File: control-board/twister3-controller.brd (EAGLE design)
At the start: 191 x 90.5 mm, 54 parts, among them J2 OSTVN04A150, J7 BARREL-JACK_PJ-063BH, U1 MAX6816, U10 Teensy 3.2, U11 TMC2130-LA, U2 GDM1602K, U3 IS31FL3193, U4 MIC4680-5.0YM-TR

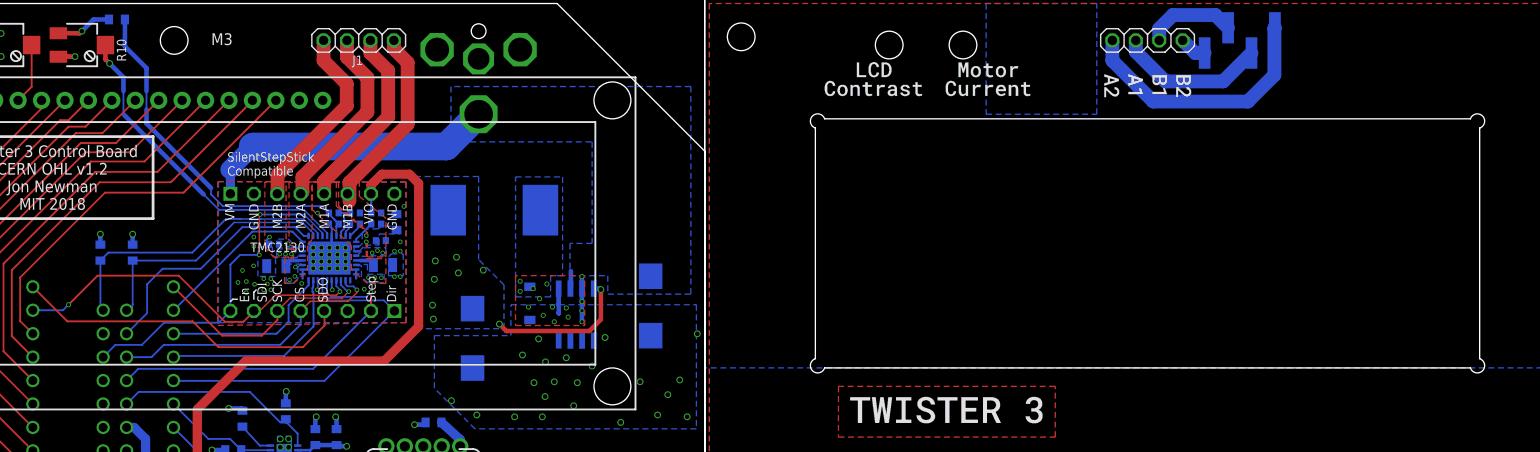
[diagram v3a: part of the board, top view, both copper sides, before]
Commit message: Small updates to control board
- Tighter tolerance on LCD cutout
- Added test points
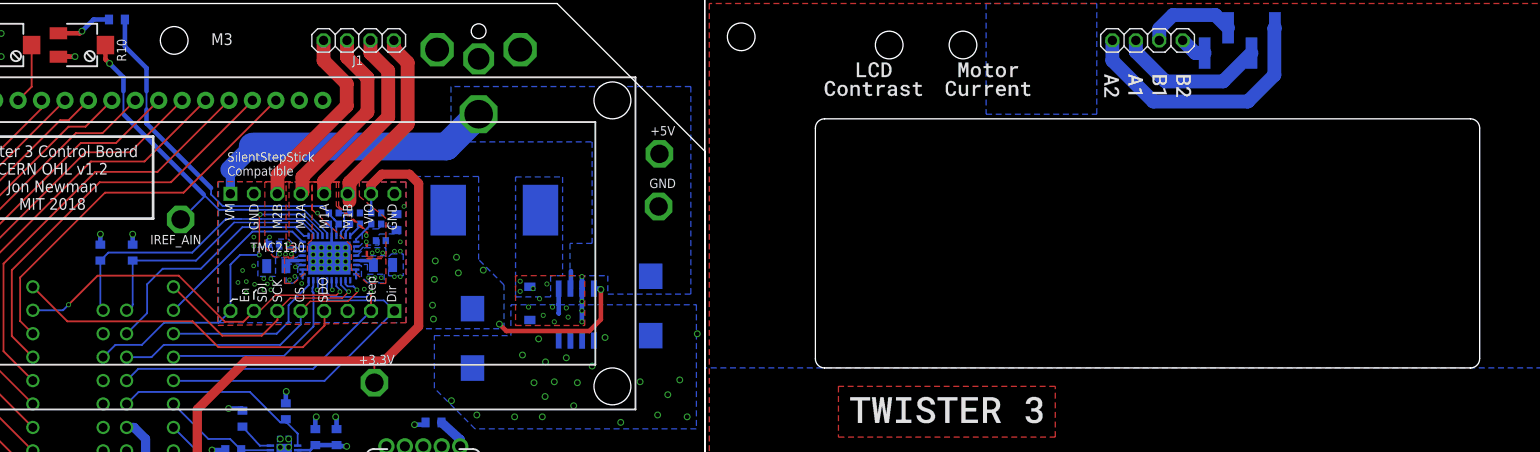
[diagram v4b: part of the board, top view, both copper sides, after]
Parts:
- added +3.3V, +5V, GND, IREF_AIN: (no value), jonnew:TESTPOINT_2MM
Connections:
- net +3V3: now also +3.3V.1
- net +5V0: now also +5V.1
- net GND: now also GND.1
- net IREF: now also IREF_AIN.1
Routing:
- net IREF: track 36.4 -> 40.1 mm
- net +3V3: track 86.4 -> 88.8 mm
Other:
- board text added: "+3.3V"
- board text added: "+5V"
- board text added: "IREF_AIN"
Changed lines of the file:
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@@
 <setting verticaltext="up"/>
 </settings>
-<grid distance="0.5" unitdist="mm" unit="mm" style="lines" multiple="1" display="yes" altdistance="5" altunitdist="mil" altunit="mil"/>
+<grid distance="0.1" unitdist="mm" unit="mm" style="lines" multiple="1" display="yes" altdistance="5" altunitdist="mil" altunit="mil"/>
 <layers>
 <layer number="1" name="Top" color="4" fill="1" visible="yes" active="yes"/>
@@
 <layer number="27" name="tValues" color="7" fill="1" visible="yes" active="yes"/>
 <layer number="28" name="bValues" color="7" fill="1" visible="yes" active="yes"/>
-<layer number="29" name="tStop" color="7" fill="3" visible="no" active="yes"/>
-<layer number="30" name="bStop" color="7" fill="6" visible="no" active="yes"/>
-<layer number="31" name="tCream" color="7" fill="4" visible="no" active="yes"/>
-<layer number="32" name="bCream" color="7" fill="5" visible="no" active="yes"/>
+<layer number="29" name="tStop" color="7" fill="3" visible="yes" active="yes"/>
+<layer number="30" name="bStop" color="7" fill="6" visible="yes" active="yes"/>
+<layer number="31" name="tCream" color="7" fill="4" visible="yes" active="yes"/>
+<layer number="32" name="bCream" color="7" fill="5" visible="yes" active="yes"/>
 <layer number="33" name="tFinish" color="6" fill="3" visible="no" active="yes"/>
 <layer number="34" name="bFinish" color="6" fill="6" visible="no" active="yes"/>
@@
 <wire x1="-1" y1="0" x2="1" y2="0" width="0.127" layer="51"/>
 <wire x1="107.5" y1="53.5" x2="107.5" y2="28.5" width="0" layer="20"/>
+<wire x1="107.5" y1="28.5" x2="108.5" y2="27.5" width="0" layer="20" curve="90"/>
 <wire x1="108.5" y1="27.5" x2="178.5" y2="27.5" width="0" layer="20"/>
+<wire x1="178.5" y1="27.5" x2="179.5" y2="28.5" width="0" layer="20" curve="90"/>
 <wire x1="179.5" y1="28.5" x2="179.5" y2="53.5" width="0" layer="20"/>
 <circle x="160.5" y="12" radius="3.3" width="0.05" layer="20"/>
 <wire x1="178.5" y1="54.5" x2="108.5" y2="54.5" width="0" layer="20"/>
-<wire x1="107.5" y1="53.5" x2="108.5" y2="54.5" width="0" layer="20" curve="-233.130102"/>
-<wire x1="108.5" y1="27.5" x2="107.5" y2="28.5" width="0" layer="20" curve="-233.130102"/>
-<wire x1="179.5" y1="28.5" x2="178.5" y2="27.5" width="0" layer="20" curve="-233.130102"/>
-<wire x1="178.5" y1="54.5" x2="179.5" y2="53.5" width="0" layer="20" curve="-233.130102"/>
 <wire x1="95.5" y1="81" x2="95.5" y2="-9.5" width="0" layer="20"/>
 <text x="92.5" y="82" size="1.778" layer="20">V-CUT</text>
@@
 <circle x="133.5" y="63" radius="3.5" width="0" layer="32"/>
 <text x="135.5" y="58" size="1.27" layer="22" font="vector" ratio="18" rot="MR0">M5</text>
+<wire x1="107.5" y1="53.5" x2="108.5" y2="54.5" width="0" layer="20" curve="-90"/>
+<wire x1="178.5" y1="54.5" x2="179.5" y2="53.5" width="0" layer="20" curve="-90"/>
+<text x="41.4" y="40.9" size="1.016" layer="22" font="vector" ratio="18" rot="MR0">IREF_AIN</text>
+<text x="61.8" y="27.8" size="1.016" layer="22" font="vector" ratio="18" rot="MR0">+3.3V</text>
+<text x="92" y="52.7" size="1.016" layer="22" font="vector" ratio="18" rot="MR0">+5V</text>
+<text x="92.4" y="46.9" size="1.016" layer="22" font="vector" ratio="18" rot="MR0">GND</text>
 </plain>
 <attributes>
@@
 <attribute name="VALUE" x="83.601971875" y="3.71381875" size="1.27" layer="27" font="vector" ratio="18" rot="R45"/>
 </element>
+<element name="GND" library="jonnew" package="TESTPOINT_2MM" value="" x="90.5" y="45" smashed="yes">
+<attribute name="NAME" x="89.5" y="47" size="1.016" layer="25" font="vector" ratio="18"/>
+<attribute name="VALUE" x="89.5" y="42" size="0.8128" layer="27" font="vector" ratio="18"/>
+</element>
+<element name="+5V" library="jonnew" package="TESTPOINT_2MM" value="" x="90.6" y="50.7" smashed="yes">
+<attribute name="NAME" x="89.6" y="52.7" size="1.016" layer="25" font="vector" ratio="18"/>
+<attribute name="VALUE" x="89.6" y="47.7" size="0.8128" layer="27" font="vector" ratio="18"/>
+</element>
+<element name="+3.3V" library="jonnew" package="TESTPOINT_2MM" value="" x="59.7" y="25.9" smashed="yes">
+<attribute name="NAME" x="58" y="27.9" size="1.016" layer="25" font="vector" ratio="18"/>
+<attribute name="VALUE" x="58.7" y="22.9" size="0.8128" layer="27" font="vector" ratio="18"/>
+</element>
+<element name="IREF_AIN" library="jonnew" package="TESTPOINT_2MM" value="" x="38.7" y="43.6" smashed="yes">
+<attribute name="NAME" x="35.4" y="40.9" size="1.016" layer="25" font="vector" ratio="18"/>
+<attribute name="VALUE" x="37.7" y="40.6" size="0.8128" layer="27" font="vector" ratio="18"/>
+</element>
 </elements>
 <signals>
@@
 <wire x1="34.9" y1="19.8" x2="34.9" y2="17.95" width="1" layer="16"/>
 <wire x1="34.9" y1="17.95" x2="33.5" y2="16.55" width="1" layer="16"/>
-<wire x1="45.75" y1="28.25" x2="60.75" y2="28.25" width="1" layer="1"/>
+<wire x1="59.6" y1="28.25" x2="45.75" y2="28.25" width="1" layer="1"/>
+<wire x1="59.6" y1="28.25" x2="60.75" y2="28.25" width="1" layer="1"/>
 <wire x1="40.5" y1="23" x2="45.75" y2="28.25" width="1" layer="1"/>
+<contactref element="+3.3V" pad="1"/>
+<wire x1="59.7" y1="25.9" x2="59.7" y2="28.008578125" width="0.2" layer="1"/>
+<wire x1="59.7" y1="28.008578125" x2="59.6" y2="28.25" width="0.2" layer="1" curve="45"/>
 </signal>
 <signal name="N$4">
@@
 <wire x1="19.25" y1="61.25" x2="17.45" y2="61.25" width="0.5" layer="1"/>
 <wire x1="17.45" y1="61.25" x2="17.45" y2="61.23" width="0.5" layer="1"/>
-<wire x1="25.27" y1="61.23" x2="25.5" y2="61.23" width="0.3" layer="1"/>
+<wire x1="25.45" y1="61.23" x2="25.5" y2="61.23" width="0.3" layer="1"/>
 <wire x1="25.45" y1="61.23" x2="25.27" y2="61.23" width="0.3" layer="1"/>
+<contactref element="GND" pad="1"/>
 </signal>
 <signal name="ENC_A">
@@
 <wire x1="46.7" y1="44.6341" x2="46.7" y2="44.6" width="0.2" layer="16"/>
 <wire x1="46.7" y1="44.6341" x2="42.8659" y2="44.6341" width="0.2" layer="16"/>
-<wire x1="42.8659" y1="44.6341" x2="41.2" y2="46.3" width="0.2" layer="16"/>
+<wire x1="41.35" y1="46.15" x2="42.8659" y2="44.6341" width="0.2" layer="16"/>
+<wire x1="41.35" y1="46.15" x2="41.2" y2="46.3" width="0.2" layer="16"/>
 <wire x1="52.07161875" y1="44.6341" x2="46.7" y2="44.6341" width="0.2" layer="16"/>
 <wire x1="54.574" y1="41.81" x2="54.574" y2="42.13171875" width="0.16" layer="16"/>
@@
 <wire x1="31" y1="60.5" x2="30.55" y2="60.95" width="0.5" layer="1"/>
 <wire x1="30.55" y1="60.95" x2="30.55" y2="62.5" width="0.5" layer="1"/>
+<contactref element="IREF_AIN" pad="1"/>
+<wire x1="38.7" y1="43.6" x2="38.870709375" y2="43.670709375" width="0.2" layer="16" curve="44.999476"/>
+<wire x1="38.870709375" y1="43.670709375" x2="41.35" y2="46.15" width="0.2" layer="16"/>
 </signal>
 <signal name="CFG-6">
@@
 <wire x1="54.1" y1="15.0636" x2="52.2236" y2="15.0636" width="0.3" layer="16"/>
 <wire x1="52.2236" y1="15.0636" x2="52.16" y2="15" width="0.3" layer="16"/>
+<contactref element="+5V" pad="1"/>
 </signal>
 <signal name="V_BM">

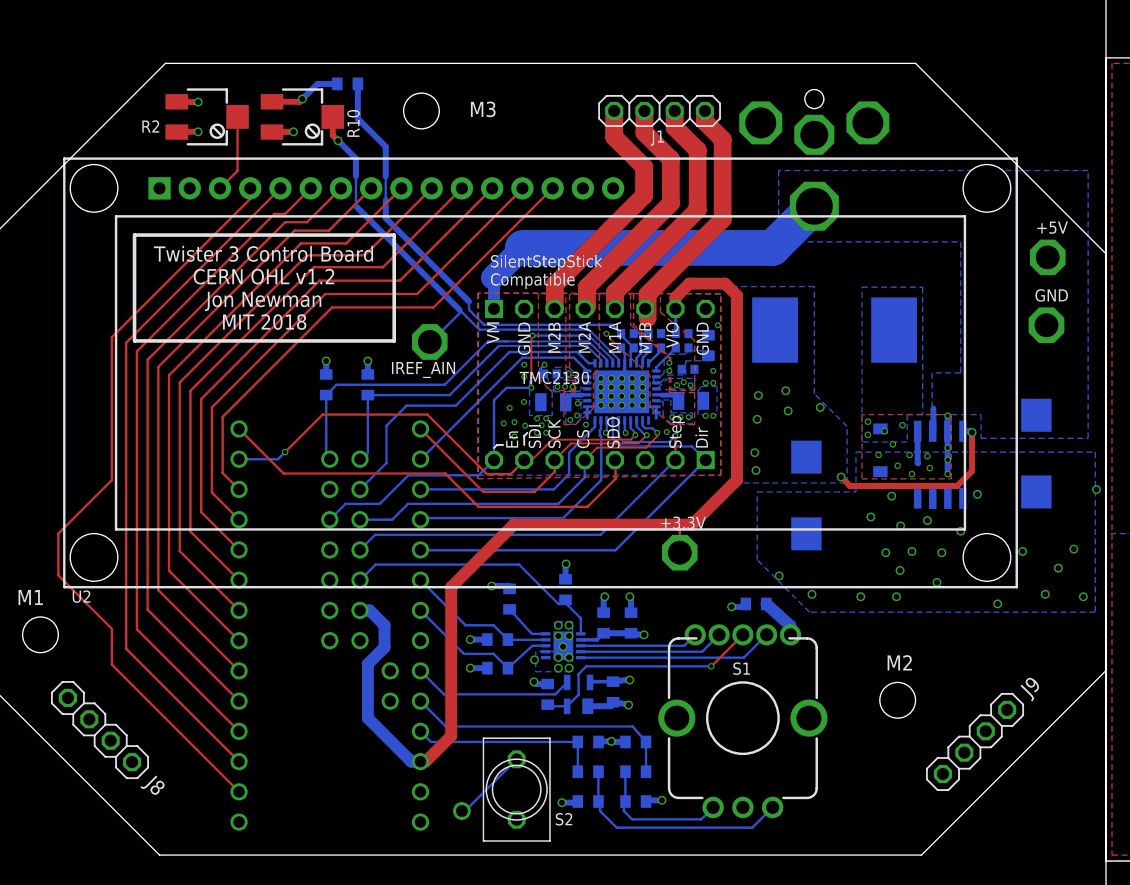
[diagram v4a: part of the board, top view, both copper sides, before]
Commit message: Updates to control board after assembly of rev 1.1
- Better retaining mechanism for top panel
- Simplified and updated BOM on the google doc to match this version
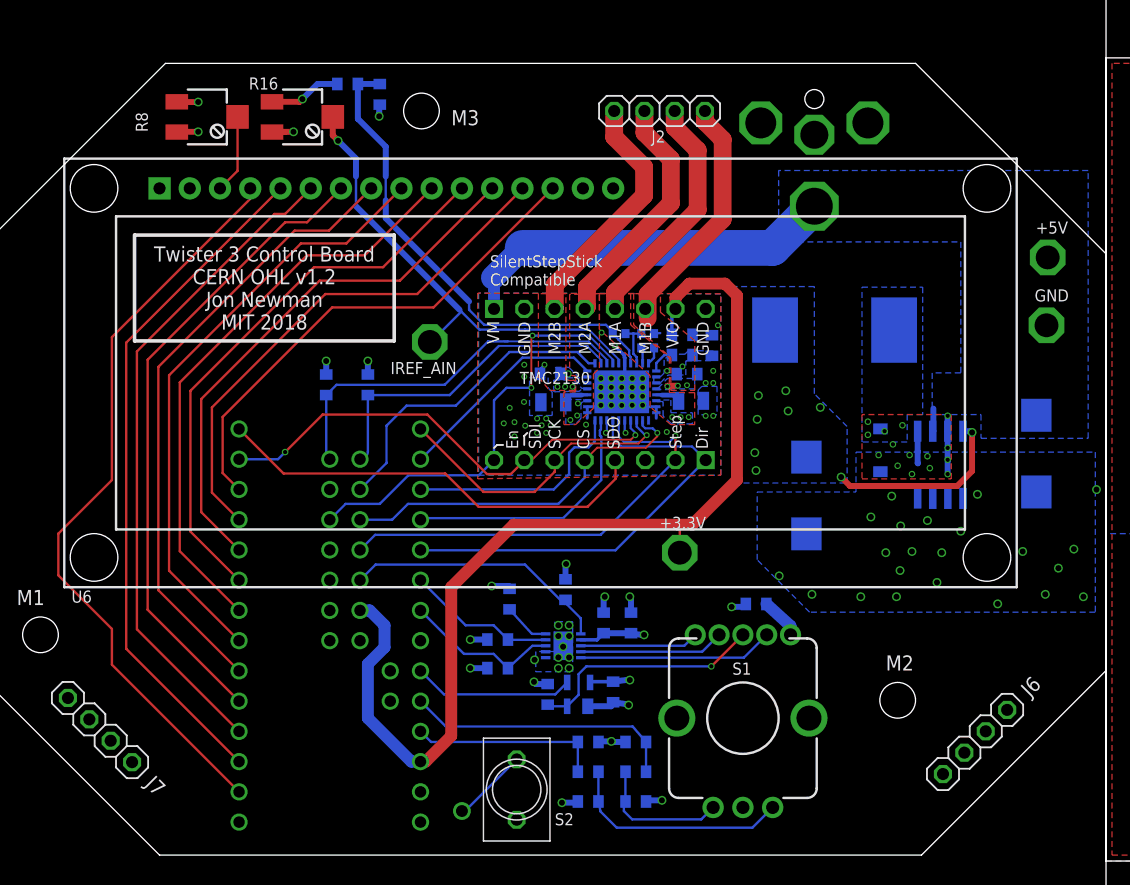
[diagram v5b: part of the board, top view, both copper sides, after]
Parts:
- removed C17: 100n/50V, jonnew:0402
- removed C18: 100nF/50V, jonnew:0402
- removed C19: 22nF/50V, jonnew:0402
- removed R18, R19: 0.11, jonnew:0805
- removed R22: 20k, jonnew:0603
- removed R23: 2.2, jonnew:0402
- removed U11: TMC2130-LA, we-chip:QFN36-PAD
- added C10, C9: 100nF/50V, jonnew:0603
- added C11: 1uF/50V, jonnew:0603
- added R11: 4.7k, cyclops:0603
- added R17: 10k, jonnew:0603
- added R8: 20k, jonnew:SM-42/43X
- added R9: 4.7k, jonnew:0603
- added U6: GDM1602K, jonnew:LCD-16X2
- C12: value 1u/50V -> 100nF/50V
- C13: value 100n/50V -> 22nF/50V
- C14: value 470nF/10V -> 1uF/50V; device jonnew:0402 -> jonnew:0603
- C15: value 47uF/10V -> 100nF/50V; device jonnew:0402 -> jonnew:0603
- C16: value 100n/50V -> 470nF/10V
- C3: value 10nF -> 1uF/50V
- C4: value 10nF -> T491D156K035AT; device jonnew:0603 -> jonnew:7343M
- C5: value 10nF -> T491D227M010AT; device jonnew:0603 -> jonnew:7343M
- C6: value 1uF -> 10nF
- C7: value T491D227M010AT -> 10nF; device jonnew:7343M -> jonnew:0603
- C8: value T491D156K035AT -> 10nF; device jonnew:7343M -> jonnew:0603
- J1: value (none) -> BARREL-JACK_PJ-063BH; device jonnew:1X04 -> jonnew:PJ-063BH
- J2: value OSTVN04A150 -> (none)
- J5: value (none) -> OSTVN04A150; device jonnew:JP4_SMD -> jonnew:1X04
- J7: value BARREL-JACK_PJ-063BH -> (none); device jonnew:PJ-063BH -> jonnew:1X04
- J8: device jonnew:1X04 -> jonnew:JP4_SMD
- R1: value 10k -> 4.7k
- R10: value 20k -> 4.7k; device jonnew:SM-42/43X -> jonnew:0603
- R12: device jonnew:0603 -> cyclops:0603
- R13: value 470 -> 20k; device cyclops:0603 -> jonnew:0603
- R14, R15: value 4.7k -> 0.11; device cyclops:0603 -> jonnew:0805
- R16: value 100k -> 20k; device jonnew:0603 -> jonnew:SM-42/43X
- R2: value 20k -> 10k; device jonnew:SM-42/43X -> jonnew:0603
- R3: value 4.7k -> 10k
- R6: value 10k -> 470; device jonnew:0603 -> cyclops:0603
- R7: value 4.7k -> 2.2; device jonnew:0603 -> jonnew:0402
- U1: value MAX6816 -> IS31FL3193; device jonnew:SOT143-4 -> jonnew:PWSON-N10-3X3
- U2: value GDM1602K -> MIC4680-5.0YM-TR; device jonnew:LCD-16X2 -> jonnew:SOIC127P500X400-8N
- U3: value IS31FL3193 -> MAX6816; device jonnew:PWSON-N10-3X3 -> jonnew:SOT143-4
- U4: value MIC4680-5.0YM-TR -> TMC2130-LA; device jonnew:SOIC127P500X400-8N -> we-chip:QFN36-PAD
- moved J8 151.7 mm to (153.5, 63.0), flipped to the bottom, turned to 180 degrees
- moved J2 85.5 mm to (58.0, 63.0), turned to 180 degrees
- moved J7 82.1 mm to (11.0, 11.0), flipped to the top, turned to 135 degrees
- moved J4 73.5 mm to (180.0, 10.0), turned to 315 degrees
- moved J3 70.1 mm to (106.5, 11.0), turned to 225 degrees
- moved R2 67.8 mm to (56.0, 5.00), flipped to the bottom, turned to 180 degrees
- moved J5 64.4 mm to (143.5, 63.0), flipped to the top, turned to 0 degrees
- moved R13 54.0 mm to (31.8, 65.3), turned to 180 degrees
- moved R10 49.1 mm to (44.4, 16.2), flipped to the bottom, turned to 180 degrees
- moved R16 45.4 mm to (28.0, 62.5), flipped to the top, turned to 270 degrees
- moved C4 40.8 mm to (89.6, 34.2)
- moved C8 40.8 mm to (54.1, 14.2)
- moved U2 34.5 mm to (81.6, 33.3), flipped to the bottom, turned to 270 degrees
- moved C14 30.6 mm to (34.5, 64.4), turned to 90 degrees
- moved R7 29.9 mm to (54.6, 44.3), turned to 0 degrees
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- renumbered J9 to J6, JP6 to J10, JP7 to J11, U10 to U5
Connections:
- net !IS31_SHDN: now also R17.1, U1.1; no longer R16.1, U3.1
- net +24V0: now also C10.1, C11.1, C4.+, C9.1, J1.1, U2.2, U4.16, U4.30, U4.31; no longer C16.1, C17.1, C18.1, C8.+, J7.1, U11.16, U11.30, U11.31, U4.2
- net +3V3: now also C15.2, U4.8; no longer C13.2, U11.8
- net +5V0: now also C2.1, C3.1, C5.+, C8.1, R10.1, R11.2, R2.2, R3.2, R8.1, R9.1, U1.2, U2.4, U3.4, U6.15, U6.2; no longer C4.1, C5.1, C6.1, C7.+, R14.2, R15.2, R2.1, R3.1, R6.2, R7.1, U1.4, U2.15, U2.2, U3.2, U4.4
- net +5VOUT: now also C14.2, R13.2, R7.2, U4.25; no longer C15.2, R22.2, R23.2, U11.25
- net BRA1: now also R15.2, U4.33; no longer R19.2, U11.33
- net BRB1: now also R14.2, U4.14; no longer R18.2, U11.14
- net BUTT: now also U3.3; no longer U1.3
- net CFG-0/MISO: now also U4.5; no longer U11.5
- net CFG-1/MOSI: now also U4.4; no longer U11.4
- net CFG-2/SCLK: now also U4.3; no longer U11.3
- net CFG-3/!TMC_CS: now also U4.2; no longer U11.2
- net CFG-6: now also U4.22; no longer U11.22
- net CFG4: now also U4.18; no longer U11.18
- net CFG5: now also U4.19; no longer U11.19
- net CPI1: now also C13.2, U4.28; no longer C19.2, U11.28
- net CPO1: now also C13.1, U4.27; no longer C19.1, U11.27
- net DB0: now also U6.7; no longer U2.7
- net DB1: now also U6.8; no longer U2.8
- net DB2: now also U6.9; no longer U2.9
- net DB3: now also U6.10; no longer U2.10
- net DB4: now also U6.11; no longer U2.11
- net DB5: now also U6.12; no longer U2.12
- net DB6: now also U6.13; no longer U2.13
- net DB7: now also U6.14; no longer U2.14
- net DIAG0: now also R11.1, U4.20; no longer R15.1, U11.20
- net DIAG1: now also R12.1, U4.21; no longer R14.1, U11.21
- net DIR: now also U4.7; no longer U11.7
- net E: now also U6.6; no longer U2.6
- net ENC_A: now also C6.1, R4.2; no longer C3.1, R5.2
- net ENC_B: now also C7.1, R5.2; no longer C2.1, R4.2
- net GND: now also C10.2, C11.2, C16.1, C4.-, C5.-, C7.2, C8.2, C9.2, J1.2, R14.1, R15.1, R16.3, R17.2, R6.1, R8.3, U1.6, U1.7, U1.PAD, U2.5, U2.6, U2.7, U2.8, U3.1, U4.11, U4.12, U4.24, U4.35, U4.36, U4.TP, U6.1, U6.16; no longer C12.2, C13.1, C16.2, C17.2, C4.2, C5.2, C7.-, C8.-, J7.2, R10.3, R13.1, R16.2, R18.1, R19.1, R2.3, U1.1, U11.1, U11.11, U11.12, U11.24, U11.35, U11.36, U11.TP, U2.16, U3.6, U3.7, U3.PAD, U4.5, U4.6, U4.7, U4.8
- net IREF: now also R16.2, U4.23; no longer R10.2, U11.23
- net MECH: now also J3.1, J3.2, J3.3, J3.4; no longer J5.1, J5.2, J5.3, J5.4
- net N$1: now also R2.1, R4.1; no longer R1.1, R5.1
- net N$10: now also U1.4; no longer U3.4
- net N$11: now also R8.2, U6.3; no longer R2.2, U2.3
- net N$2: now also R6.2, U3.2; no longer R13.2, U1.2
- net N$3: now also U1.3; no longer U3.3
- net N$4: now also R3.1, R5.1; no longer R4.1, R6.1
- net N$6: now also J5.1, J8.4; no longer J2.1, J3.4
- net N$7: now also J5.2, J8.3; no longer J2.2, J3.3
- net N$8: now also J5.3, J8.2; no longer J2.3, J3.2
- net N$9: now also J5.4, J8.1; no longer J2.4, J3.1
- net OA1: now also J2.2, U4.34; no longer J1.2, U11.34
- net OA2: now also J2.1, U4.32; no longer J1.1, U11.32
- net OB1: now also J2.3, U4.13; no longer J1.3, U11.13
- net OB2: now also J2.4, U4.15; no longer J1.4, U11.15
- net RS: now also U6.4; no longer U2.4
- net RW: now also U6.5; no longer U2.5
- net SCL: now also R10.2, U1.8; no longer R7.2, U3.8
- net SDA: now also R9.2, U1.9; no longer R3.2, U3.9
- net SD_MODE: now also U4.9; no longer U11.9
- net SPI_MODE: now also U4.10; no longer U11.10
- net STEP: now also U4.6; no longer U11.6
- net SUPPY4: now also U1.5; no longer U3.5
- net SW: now also U2.3; no longer U4.3
- net VCC1: now also C16.2, R7.1, U4.26; no longer C14.2, R23.1, U11.26
- net VCP1: now also C12.2, U4.29; no longer C18.2, U11.29
- net VREF2: now also R13.1, R16.1; no longer R10.1, R22.1
- net V_BM: now also R1.1, U1.10; no longer R12.1, U3.10
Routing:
- net GND: track 27.9 -> 29.5 mm, vias 85 -> 87
- net +5VOUT: track 39.7 -> 40.8 mm
- net OA2: track 20.6 -> 21.6 mm
- net +24V0: track 36.7 -> 36.0 mm
- net SPI_MODE: track 18.4 -> 19.1 mm
- net VCP1: track 2.87 -> 2.26 mm
